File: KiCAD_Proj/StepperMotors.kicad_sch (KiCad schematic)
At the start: 2 parts, among them U3 TMC2209_MotorDriver, U4 TMC2209_MotorDriver

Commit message: Finished schematic, in review
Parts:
- added C15, C17: 100uF 50V, Capacitor_SMD:CP_Elec_8x10, symbol Device:C_Polarized
- added C16, C18: 100nF 50V, Capacitor_SMD:C_0805_2012Metric_Pad1.18x1.45mm_HandSolder, symbol Device:C
- added JP2, JP3, JP4, JP5: Jumper_2_Open, Jumper:SolderJumper-2_P1.3mm_Open_RoundedPad1.0x1.5mm, symbol Jumper:Jumper_2_Open
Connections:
- net GND: now also C15.2, C16.2, C17.2, C18.2
- net at U3.14 (MS2): now also JP3.2 (B)
- net at U3.15 (MS1): now also JP2.2 (B)
- net 3.3V+: now reaches U3.2 (VIO)
- net 3.3V+: now also U4.2 (VIO), C16.1, C18.1, JP2.1 (A), JP3.1 (A), JP4.1 (A), JP5.1 (A)
- net 12V+: now reaches U3.8 (VM)
- net 12V+: now also U4.8 (VM), C15.1, C17.1
- net at U4.14 (MS2): now also JP5.2 (B)
- net at U4.15 (MS1): now also JP4.2 (B)
- no-connect marks 0 -> 4
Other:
- note removed: "MS1/MS2 connectie?? Zie datasheet 3.4 VIO / VM??"
- company: (none) -> HAN Univeristy of Applied Sciences
- title: (none) -> Project_Healthbot_HAT
- moved on the sheet: U4

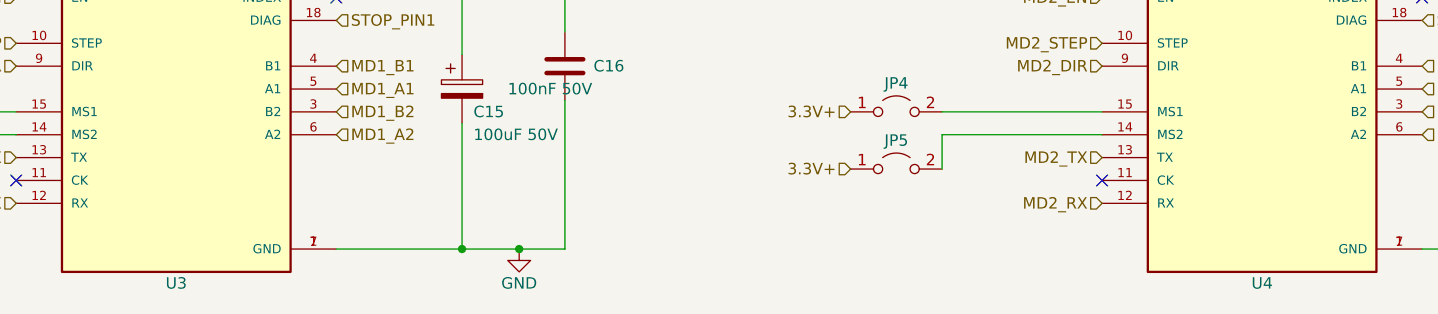
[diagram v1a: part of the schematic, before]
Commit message: -add missing connections in schematic, and some other small changes
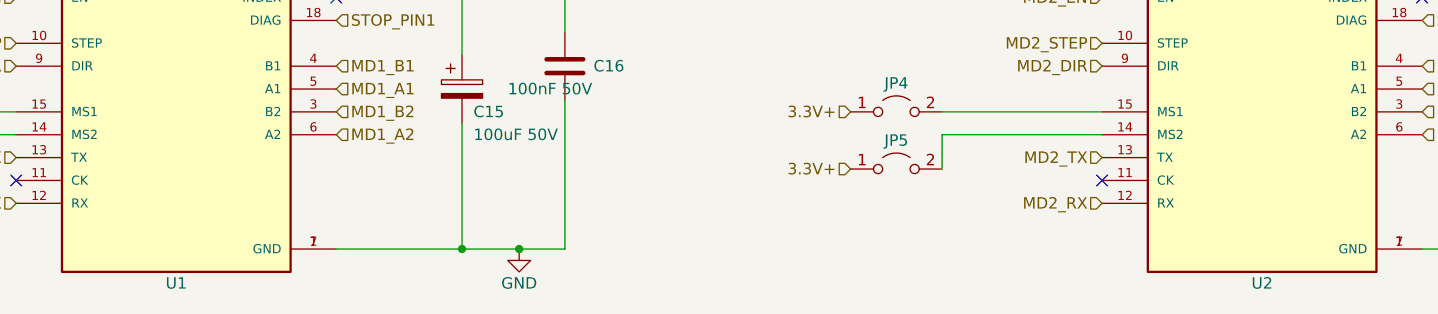
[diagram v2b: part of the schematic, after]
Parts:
- renumbered U3 to U1, U4 to U2

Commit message: Schematic finished
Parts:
- removed C15, C17: 100uF 50V, Capacitor_SMD:CP_Elec_8x10, symbol Device:C_Polarized
- removed U1, U2: TMC2209_MotorDriver, TMC2209_SILENTSTEPSTICK:MODULE_TMC2209_SILENTSTEPSTICK, symbol projectLib:TMC2209_MotorDriver
- added C15, C17: Elec_Capacitor, SamacSys_Parts:CAPAE1000X1050N, symbol Healthbot-Symbols:Elec_Capacitor
- added U1, U2: TMC2209_MotorDriver, Healthbot-Footprints:MODULE_TMC2209_SILENTSTEPSTICK, symbol Healthbot-Symbols:TMC2209_MotorDriver
- C16, C18: footprint Capacitor_SMD:C_0805_2012Metric_Pad1.18x1.45mm_HandSolder -> Capacitor_SMD:C_0603_1608Metric_Pad1.08x0.95mm_HandSolder
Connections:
- net GND: now also C15.2 (-), C17.2 (-), U1.1 (GND), U1.7 (GND), U2.1 (GND), U2.7 (GND)
- net MD1_A1: now also U1.5 (A1)
- net MD1_A2: now also U1.6 (A2)
- net MD1_B1: now also U1.4 (B1)
- net MD1_B2: now also U1.3 (B2)
- net MD1_DIR: now also U1.9 (DIR)
- net MD1_EN: now also U1.16 (~{EN})
- net MD1_RX: now also U1.12 (RX)
- net MD1_STEP: now also U1.10 (STEP)
- net MD1_TX: now also U1.13 (TX)
- net MD2_A1: now also U2.5 (A1)
- net MD2_A2: now also U2.6 (A2)
- net MD2_B1: now also U2.4 (B1)
- net MD2_B2: now also U2.3 (B2)
- net MD2_DIR: now also U2.9 (DIR)
- net MD2_EN: now also U2.16 (~{EN})
- net MD2_RX: now also U2.12 (RX)
- net MD2_STEP: now also U2.10 (STEP)
- net MD2_TX: now also U2.13 (TX)
- net STOP_PIN1: now also U1.18 (DIAG)
- net STOP_PIN2: now also U2.18 (DIAG)
- net at JP5.2 (B): now also U2.14 (MS2)
- net at JP4.2 (B): now also U2.15 (MS1)
- net at JP3.2 (B): now also U1.14 (MS2)
- net at JP2.2 (B): now also U1.15 (MS1)
- net 3.3V+ renamed +3.3V
- net +3.3V: now also U1.2 (VIO), U2.2 (VIO)
- new net +12V: C15.1 (+), C17.1 (+), U1.8 (VM), U2.8 (VM)
